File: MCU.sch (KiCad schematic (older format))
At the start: 45 parts, among them J2 JTAG, SW1 Reset, U6 STM32F303RETx, U7 MAX7375AXR805

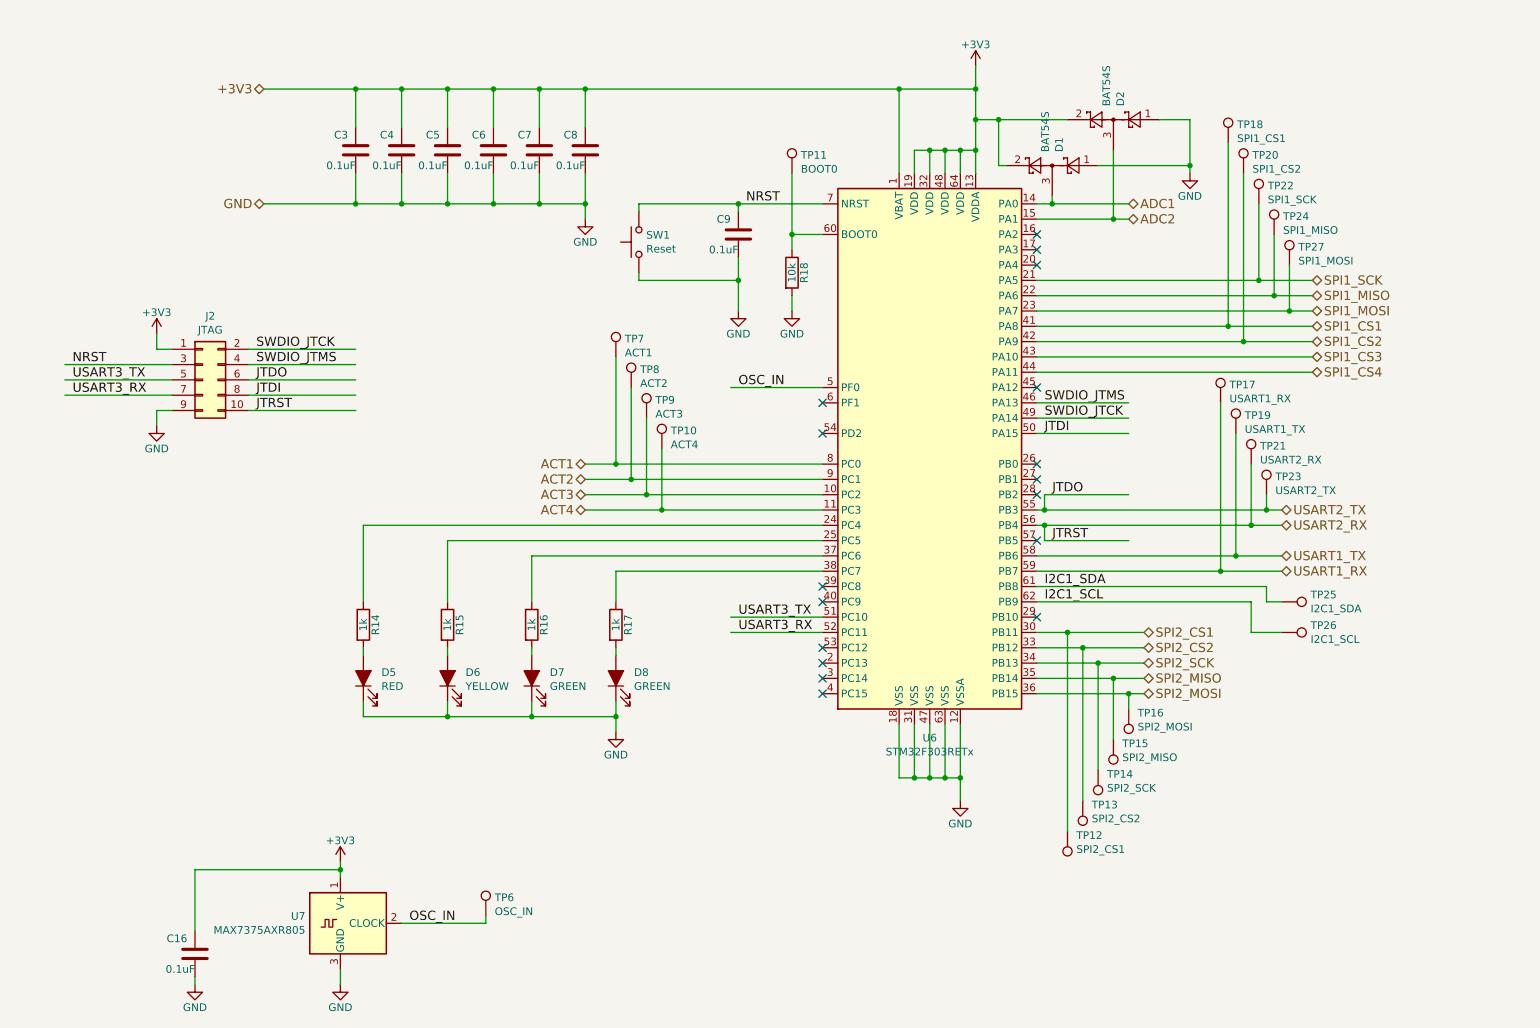
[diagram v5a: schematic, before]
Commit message: Added 10R series termination resistors to high-speed digital lines Added reverse-power protection diode Added ADC filter capacitors Added I2C pullups Added individual polyfuses to pyro drivers Changed UBSEDS logo to smaller variant Reduced LED resistors to 470R Reduced most SMD footprints to 0603 Minor schematic cleanup
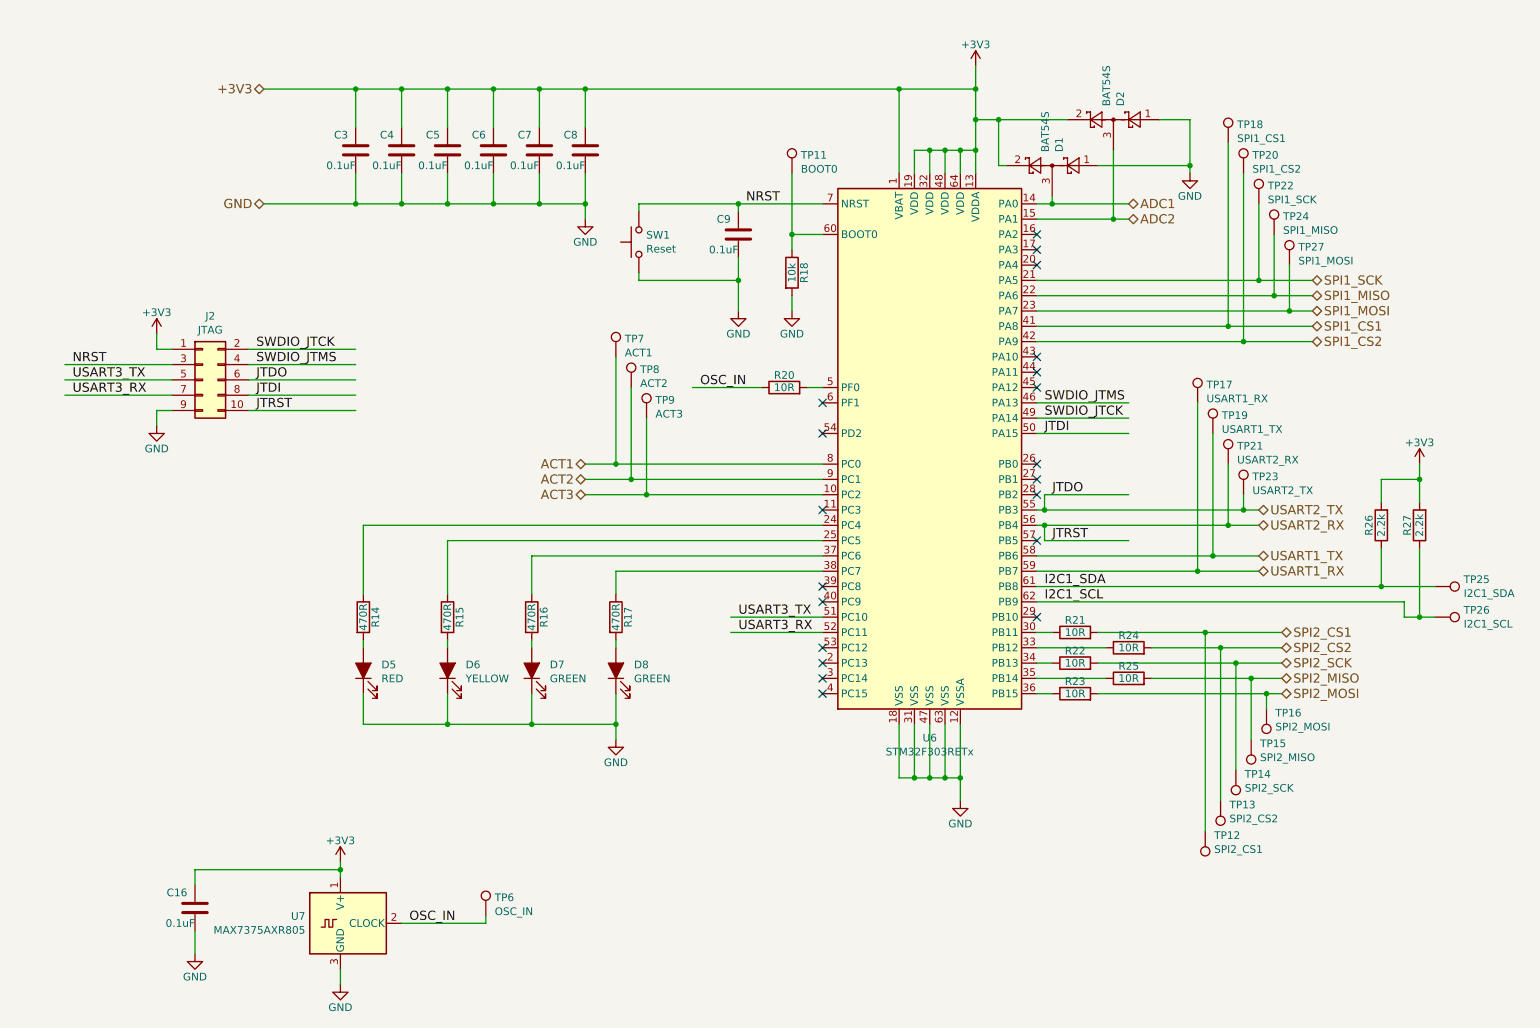
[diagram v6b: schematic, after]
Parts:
- removed TP10: ACT4, TestPoint:TestPoint_Pad_D1.0mm, symbol Connector:TestPoint
- added R20, R21, R22, R23, R24, R25: 10R, Resistor_SMD:R_0603_1608Metric_Pad1.05x0.95mm_HandSolder, symbol Device:R
- added R26, R27: 2.2k, Resistor_SMD:R_0603_1608Metric_Pad1.05x0.95mm_HandSolder, symbol Device:R
- R14, R15, R16, R17: value 1k -> 470R; footprint Resistor_SMD:R_1206_3216Metric_Pad1.42x1.75mm_HandSolder -> Resistor_SMD:R_0603_1608Metric_Pad1.05x0.95mm_HandSolder
- R18: footprint Resistor_SMD:R_1206_3216Metric_Pad1.42x1.75mm_HandSolder -> Resistor_SMD:R_0603_1608Metric_Pad1.05x0.95mm_HandSolder
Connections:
- net labels removed: ACT4, SPI1_CS3, SPI1_CS4
- wire segments 190 -> 197
- no-connect marks 17 -> 20
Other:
- moved on the sheet: C16, D5, D6, D7, D8, R14, R15, R16, R17, TP12, TP13, TP14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

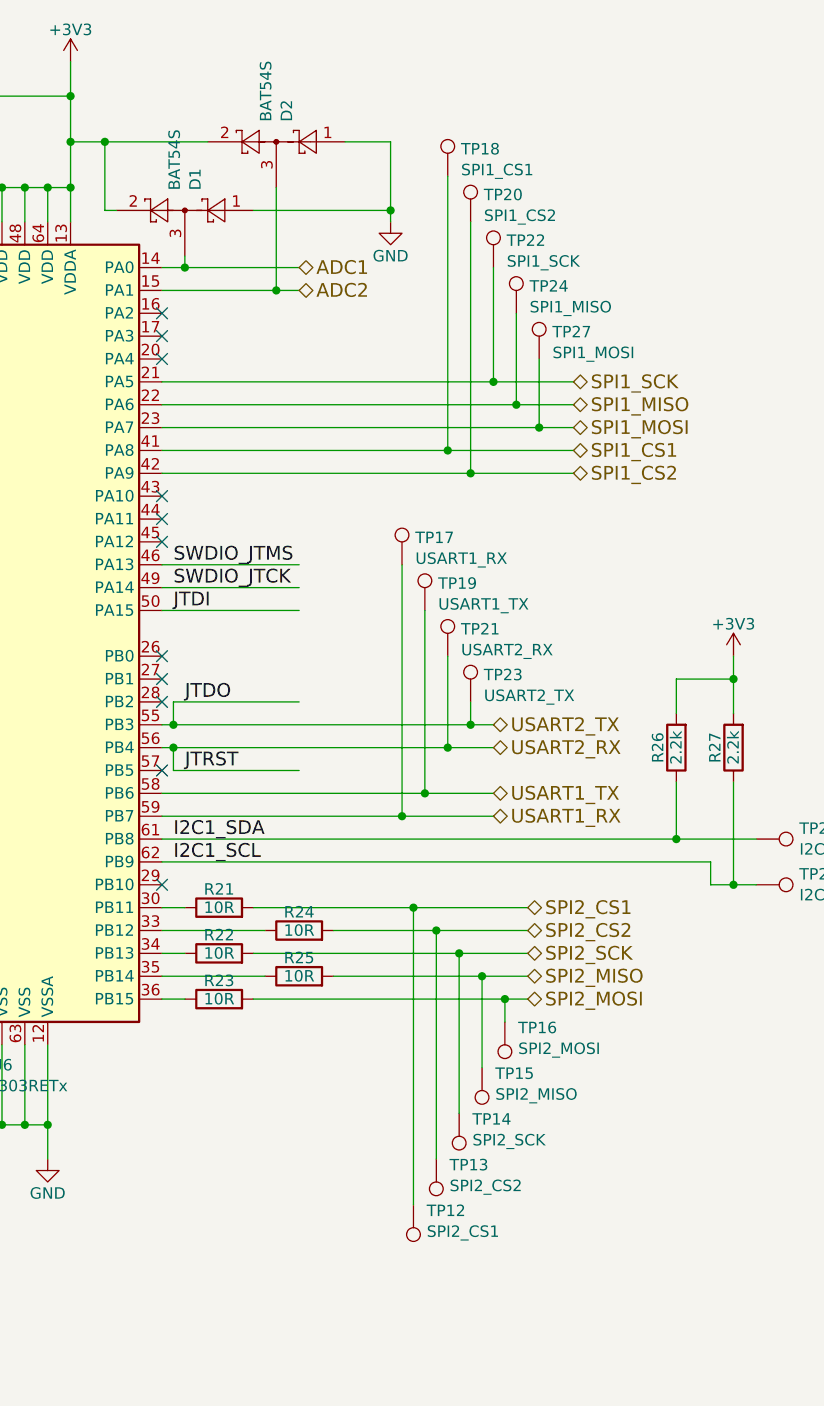
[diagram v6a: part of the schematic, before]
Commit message: Routing complete Removed some test points (couldn't easily place)
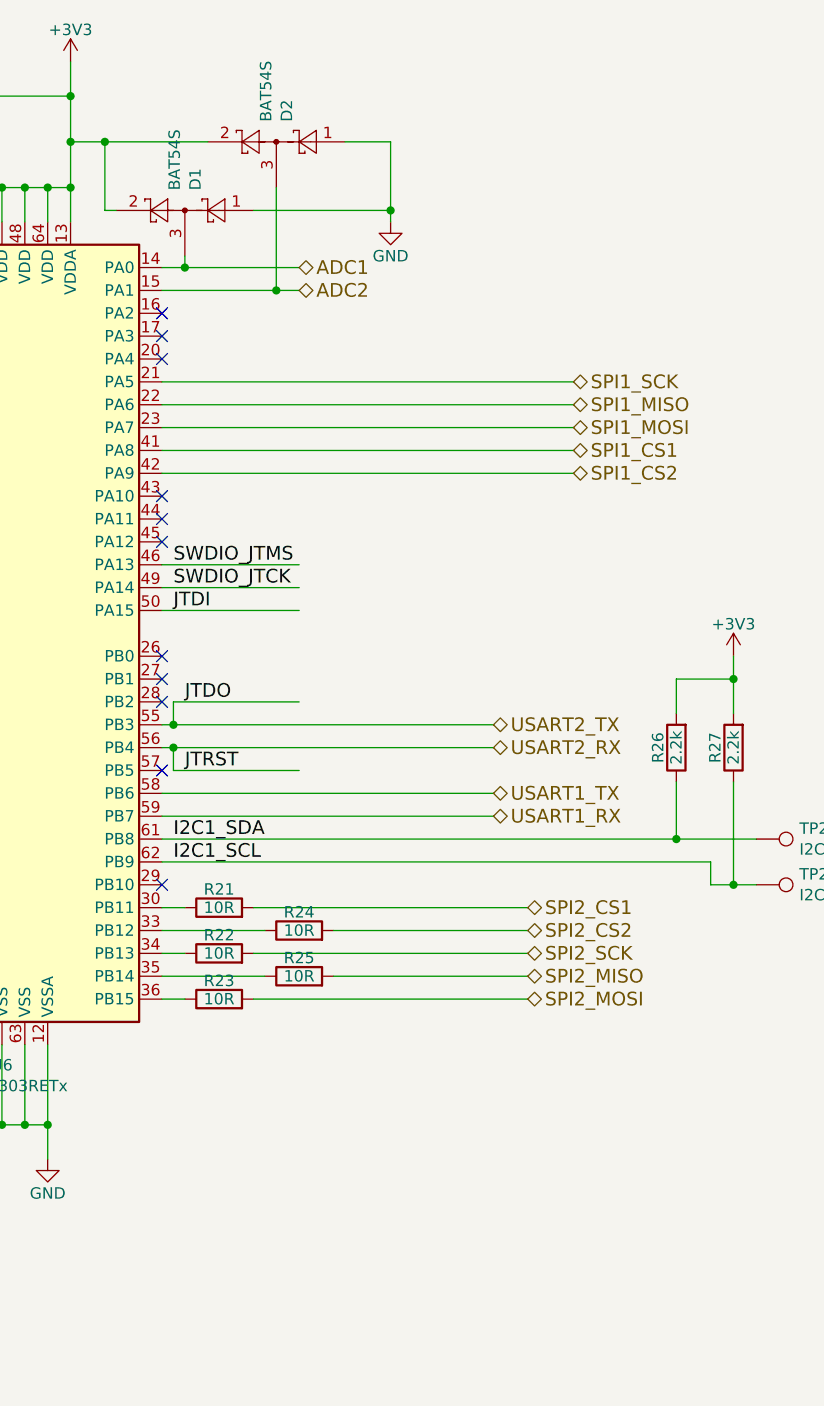
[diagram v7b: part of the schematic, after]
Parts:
- removed TP12: SPI2_CS1, TestPoint:TestPoint_Pad_D1.0mm, symbol Connector:TestPoint
- removed TP13: SPI2_CS2, TestPoint:TestPoint_Pad_D1.0mm, symbol Connector:TestPoint
- removed TP14: SPI2_SCK, TestPoint:TestPoint_Pad_D1.0mm, symbol Connector:TestPoint
- removed TP15: SPI2_MISO, TestPoint:TestPoint_Pad_D1.0mm, symbol Connector:TestPoint
- removed TP16: SPI2_MOSI, TestPoint:TestPoint_Pad_D1.0mm, symbol Connector:TestPoint
- removed TP17: USART1_RX, TestPoint:TestPoint_Pad_D1.0mm, symbol Connector:TestPoint
- removed TP18: SPI1_CS1, TestPoint:TestPoint_Pad_D1.0mm, symbol Connector:TestPoint
- removed TP19: USART1_TX, TestPoint:TestPoint_Pad_D1.0mm, symbol Connector:TestPoint
- removed TP20: SPI1_CS2, TestPoint:TestPoint_Pad_D1.0mm, symbol Connector:TestPoint
- removed TP21: USART2_RX, TestPoint:TestPoint_Pad_D1.0mm, symbol Connector:TestPoint
- removed TP22: SPI1_SCK, TestPoint:TestPoint_Pad_D1.0mm, symbol Connector:TestPoint
- removed TP23: USART2_TX, TestPoint:TestPoint_Pad_D1.0mm, symbol Connector:TestPoint
- removed TP24: SPI1_MISO, TestPoint:TestPoint_Pad_D1.0mm, symbol Connector:TestPoint
- removed TP27: SPI1_MOSI, TestPoint:TestPoint_Pad_D1.0mm, symbol Connector:TestPoint
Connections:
- wire segments 197 -> 169

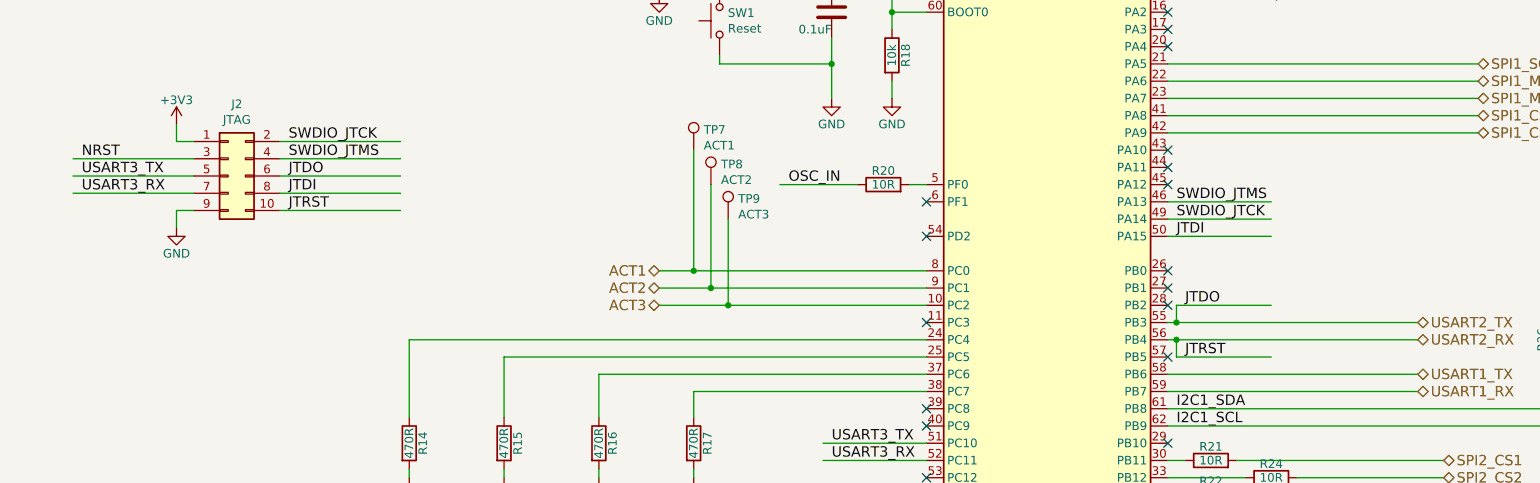
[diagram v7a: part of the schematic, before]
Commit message: Fixed silk Fixed JTAG Added PAYLOAD connector with I2C
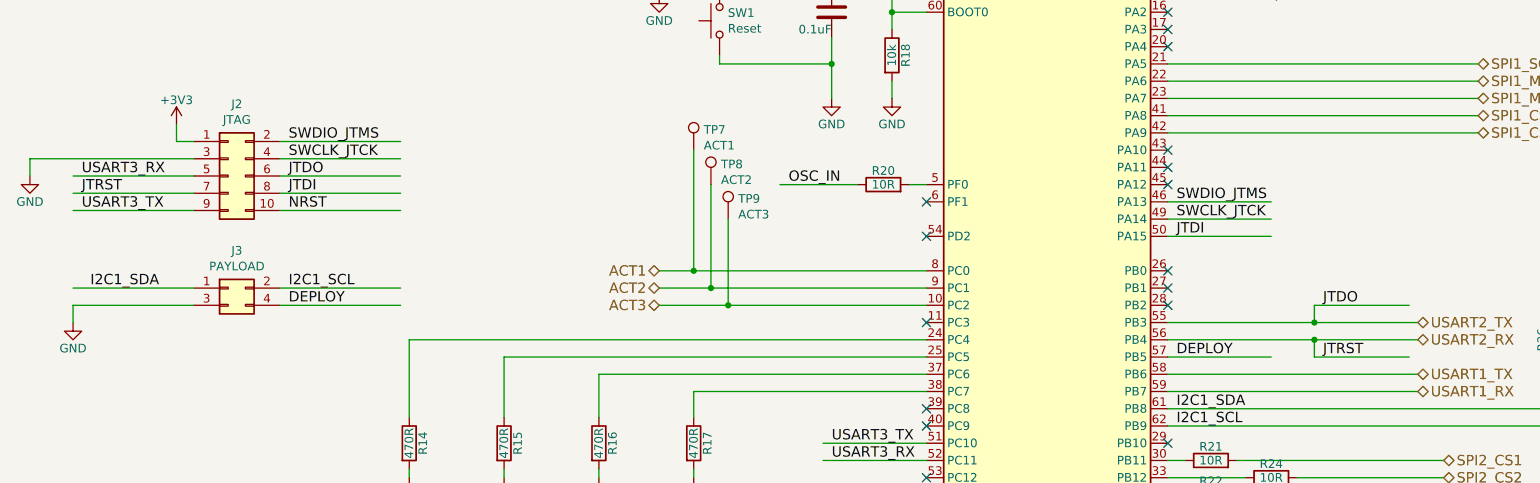
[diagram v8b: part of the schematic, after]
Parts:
- added J3: PAYLOAD, Connector_PinHeader_1.27mm:PinHeader_2x02_P1.27mm_Vertical, symbol Connector_Generic:Conn_02x02_Odd_Even
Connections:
- net labels added: DEPLOY, SWCLK_JTCK
- net labels removed: SWDIO_JTCK
- wire segments 169 -> 175
- no-connect marks 20 -> 19
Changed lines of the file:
@@
 Wire Wire Line
 	6350 1400 6850 1400
-Wire Wire Line
-	7250 4150 7300 4150
-Wire Wire Line
-	7250 4250 7300 4250
 $Comp
 L Diode:BAT54S D2
@@
 SWDIO_JTMS
 Text Label 7300 3550 0    60   ~ 0
-SWDIO_JTCK
+SWCLK_JTCK
 Text Label 7300 3650 0    60   ~ 0
 JTDI
 Wire Wire Line
-	7300 4250 7300 4350
-Wire Wire Line
-	7300 4350 7850 4350
-Connection ~ 7300 4250
-Text Label 7350 4350 0    60   ~ 0
+	8100 4250 8100 4350
+Wire Wire Line
+	8100 4350 8650 4350
+Text Label 8150 4350 0    60   ~ 0
 JTRST
 Wire Wire Line
-	2100 3200 2800 3200
-Wire Wire Line
-	2800 3100 2100 3100
+	2100 3100 2800 3100
+Wire Wire Line
+	2800 3200 2100 3200
+Text Label 2150 3100 0    60   ~ 0
+SWDIO_JTMS
 Text Label 2150 3200 0    60   ~ 0
-SWDIO_JTMS
-Text Label 2150 3100 0    60   ~ 0
-SWDIO_JTCK
+SWCLK_JTCK
 Text Label 5350 2150 0    60   ~ 0
 NRST
 Wire Wire Line
-	7300 4150 7300 4050
-Connection ~ 7300 4150
-Wire Wire Line
-	7300 4050 7850 4050
-Text Label 7350 4050 0    60   ~ 0
+	8100 4150 8100 4050
+Wire Wire Line
+	8100 4050 8650 4050
+Text Label 8150 4050 0    60   ~ 0
 JTDO
-Text Label 950  3200 0    60   ~ 0
-NRST
 Wire Wire Line
 	2200 2150 2800 2150
@@
 NoConn ~ 5850 5050
 NoConn ~ 7250 4850
-NoConn ~ 7250 4350
 NoConn ~ 7250 4050
 NoConn ~ 5850 5150
@@
 	2800 3300 2100 3300
 $Comp
-L power:GND #PWR030
-U 1 1 5E3B7BFA
-P 1500 3600
-F 0 "#PWR030" H 1500 3350 50  0001 C CNN
-F 1 "GND" H 1500 3450 50  0000 C CNN
-F 2 "" H 1500 3600 50  0001 C CNN
-F 3 "" H 1500 3600 50  0001 C CNN
-	1    1500 3600
-	1    0    0    -1
-$EndComp
-$Comp
 L power:+3V3 #PWR029
 U 1 1 5E3BE166
@@
 Text Label 2150 3400 0    60   ~ 0
 JTDI
-Text Label 2150 3500 0    60   ~ 0
-JTRST
 Wire Wire Line
 	2100 3400 2800 3400
 Wire Wire Line
-	2100 3500 2800 3500
-Wire Wire Line
 	1600 3100 1500 3100
 Wire Wire Line
 	1500 3100 1500 3000
 Wire Wire Line
-	1600 3500 1500 3500
-Wire Wire Line
-	1500 3500 1500 3600
-Wire Wire Line
-	1600 3200 900  3200
-Wire Wire Line
-	1600 3300 900  3300
-Wire Wire Line
-	1600 3400 900  3400
-Text Label 950  3300 0    60   ~ 0
+	1600 3500 900  3500
+Text Label 950  3500 0    60   ~ 0
 USART3_TX
-Text Label 950  3400 0    60   ~ 0
-USART3_RX
 $Comp
 L Connector_Generic:Conn_02x05_Odd_Even J2
@@
 	7250 4450 8700 4450
 Wire Wire Line
-	7300 4250 8700 4250
-Wire Wire Line
-	7300 4150 8700 4150
-Wire Wire Line
 	8000 5250 8850 5250
 Wire Wire Line
@@
 Wire Wire Line
 	7250 2950 9050 2950
+Wire Wire Line
+	650  3200 650  3300
+$Comp
+L power:GND #PWR030
+U 1 1 5E3B7BFA
+P 650 3300
+F 0 "#PWR030" H 650 3050 50  0001 C CNN
+F 1 "GND" H 650 3150 50  0000 C CNN
+F 2 "" H 650 3300 50  0001 C CNN
+F 3 "" H 650 3300 50  0001 C CNN
+	1    650  3300
+	1    0    0    -1
+$EndComp
+Text Label 950  3300 0    60   ~ 0
+USART3_RX
+Wire Wire Line
+	1600 3300 900  3300
+Wire Wire Line
+	900  3400 1600 3400
+Text Label 950  3400 0    60   ~ 0
+JTRST
+Text Label 2150 3500 0    60   ~ 0
+NRST
+Wire Wire Line
+	2800 3500 2100 3500
+Wire Wire Line
+	650  3200 1600 3200
+$Comp
+L Connector_Generic:Conn_02x02_Odd_Even J3
+U 1 1 5E4CC11F
+P 1800 3950
+F 0 "J3" H 1850 4167 50  0000 C CNN
+F 1 "PAYLOAD" H 1850 4076 50  0000 C CNN
+F 2 "Connector_PinHeader_1.27mm:PinHeader_2x02_P1.27mm_Vertical" H 1800 3950 50  0001 C CNN
+F 3 "~" H 1800 3950 50  0001 C CNN
+	1    1800 3950
+	1    0    0    -1
+$EndComp
+Wire Wire Line
+	2100 3950 2800 3950
+Wire Wire Line
+	2100 4050 2800 4050
+Wire Wire Line
+	1600 3950 900  3950
+Wire Wire Line
+	1600 4050 900  4050
+Wire Wire Line
+	7250 4350 7850 4350
+Text Label 7300 4350 0    60   ~ 0
+DEPLOY
+$Comp
+L power:GND #PWR0117
+U 1 1 5E523023
+P 900 4150
+F 0 "#PWR0117" H 900 3900 50  0001 C CNN
+F 1 "GND" H 900 4000 50  0000 C CNN
+F 2 "" H 900 4150 50  0001 C CNN
+F 3 "" H 900 4150 50  0001 C CNN
+	1    900  4150
+	1    0    0    -1
+$EndComp
+Wire Wire Line
+	900  4050 900  4150
+Text Label 1000 3950 0    60   ~ 0
+I2C1_SDA
+Text Label 2150 3950 0    60   ~ 0
+I2C1_SCL
+Text Label 2150 4050 0    60   ~ 0
+DEPLOY
+Connection ~ 8100 4250
+Wire Wire Line
+	8100 4250 8700 4250
+Wire Wire Line
+	7250 4250 8100 4250
+Connection ~ 8100 4150
+Wire Wire Line
+	8100 4150 8700 4150
+Wire Wire Line
+	7250 4150 8100 4150
 $EndSCHEMATC
